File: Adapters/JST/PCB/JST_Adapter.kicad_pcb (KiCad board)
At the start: 2 copper layers, 30.8 x 38 mm, 8 parts, among them J1 S4B-PH-SM4-TB(LF)(SN), J2 S6B-PH-SM4-TB(LF)(SN), P1 CONN_02X08

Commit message: adapter finished
finished adapter
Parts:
- moved FD3 32.1 mm to (101.2, 25.2)
- moved FD2 15.5 mm to (116.8, 25.2)
- moved FD1 1.50 mm to (116.8, 60.8)
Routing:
- net GND: track 0.00 -> 137.8 mm, vias 0 -> 17
- net /SPI2_NSS: track 0.00 -> 40.5 mm
- net /SPI2_SCLK: track 0.00 -> 39.8 mm
- net /SPI2_MISO: track 0.00 -> 37.3 mm
- net /SPI2_MOSI: track 0.00 -> 35.8 mm
- net /VIN: track 0.00 -> 33.4 mm
- net /USART1_RX: track 0.00 -> 20.6 mm
- net /USART1_TX: track 0.00 -> 16.0 mm
- added copper zone on B.Cu, net GND
- added copper zone on F.Cu, net GND
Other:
- net class Default: clearance 0.2 -> 0.1524; trace_width 0.25 -> 0.1524; via_dia 0.8 -> 0.635; via_drill 0.4 -> 0.3302
- rule trace_clearance: 0.2 -> 0.1524
- rule trace_min: 0.2 -> 0.1524
- rule via_min_drill: 0.3 -> 0.3302
- rule via_min_size: 0.4 -> 0.635
- board text added: "GND"
- board text added: "S1G-RF USART/SPI Adapter CERN OSHWL v1.2 Nov 2016 Designed by adamjvr"
- board text added: "SPI_MISO"
- board text added: "SPI_MOSI"
- board text added: "SPI_NSS"
- board text added: "SPI_SCLK"
- board text added: "USART_RX"
- board text added: "USART_TX"
- board text added: "VIN"

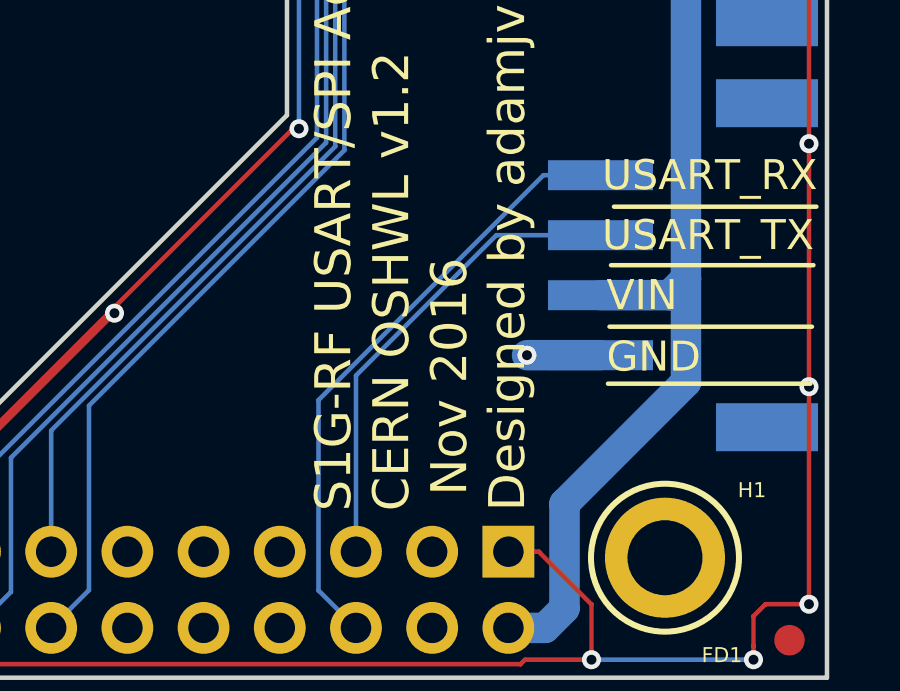
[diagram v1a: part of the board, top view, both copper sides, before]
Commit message: Via Stitching
Ground pour stiching applied to the combined PA/LNA match version of the
915MHZ radio. All ground pours and layers are now stiched together
effectively.
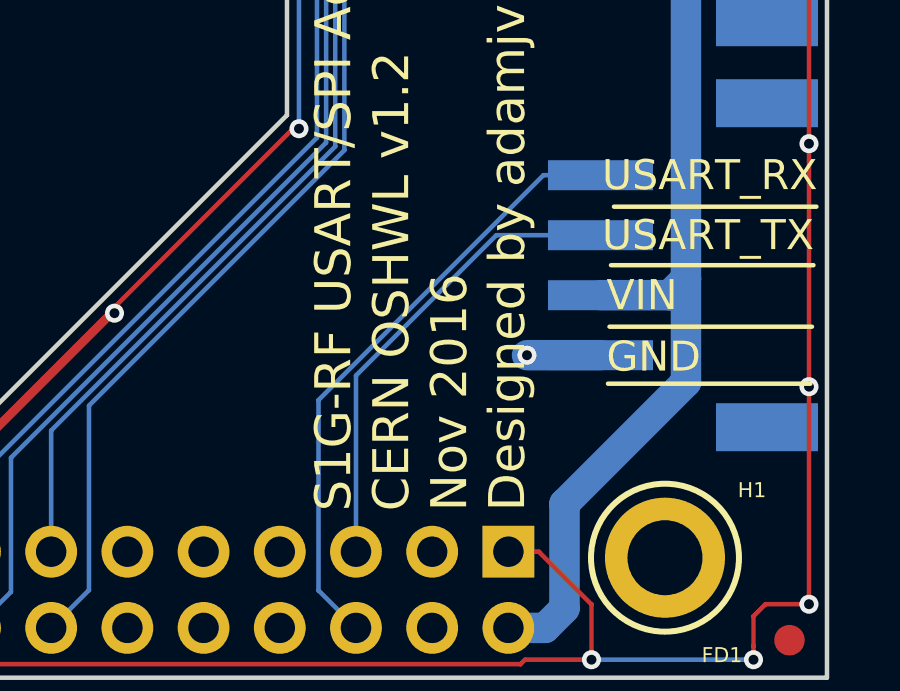
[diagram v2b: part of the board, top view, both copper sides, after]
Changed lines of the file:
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@@
   (gr_line (start 110.85 30.7) (end 117.6 30.7) (layer F.SilkS) (width 0.15))
   (gr_line (start 110.95 28.75) (end 117.7 28.75) (layer F.SilkS) (width 0.15))
-  (gr_text "S1G-RF USART/SPI Adapter\nCERN OSHWL v1.2\n Nov 2016\nDesigned by adamjvr" (at 104.45 56.45 90) (layer F.SilkS)
+  (gr_text "S1G-RF USART/SPI Adapter\nCERN OSHWL v1.2\nNov 2016\nDesigned by adamjvr" (at 104.45 56.45 90) (layer F.SilkS)
     (effects (font (size 1.2 1.2) (thickness 0.25)) (justify left))
   )

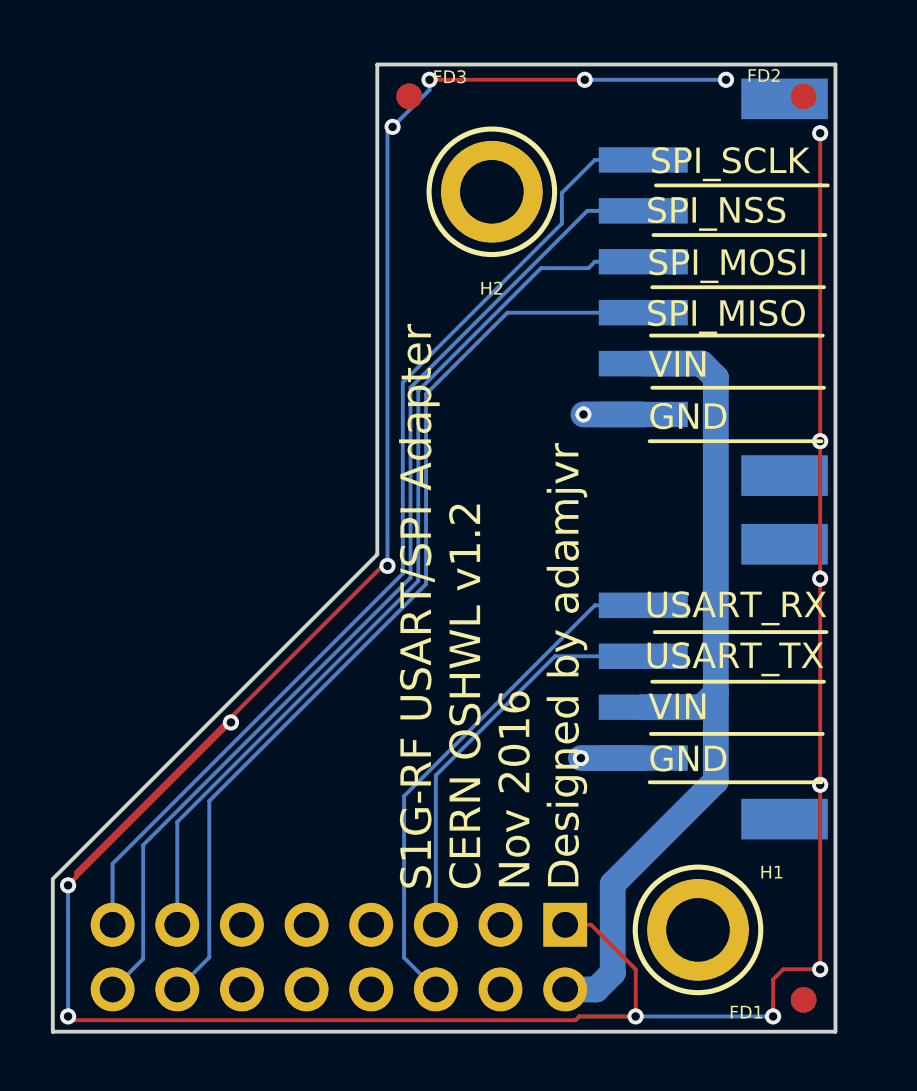
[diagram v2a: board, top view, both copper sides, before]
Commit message: Adapters
Adapter ended up being too large. So I split it into two separate
adapters one for SPI and one for USART over JST connectors. SPI board
has 100 ohm inline resistors for EMI and impedance matching in case the
driving device lacks these internally or on its board.  Additional
Fudicials added to the combined implementation.
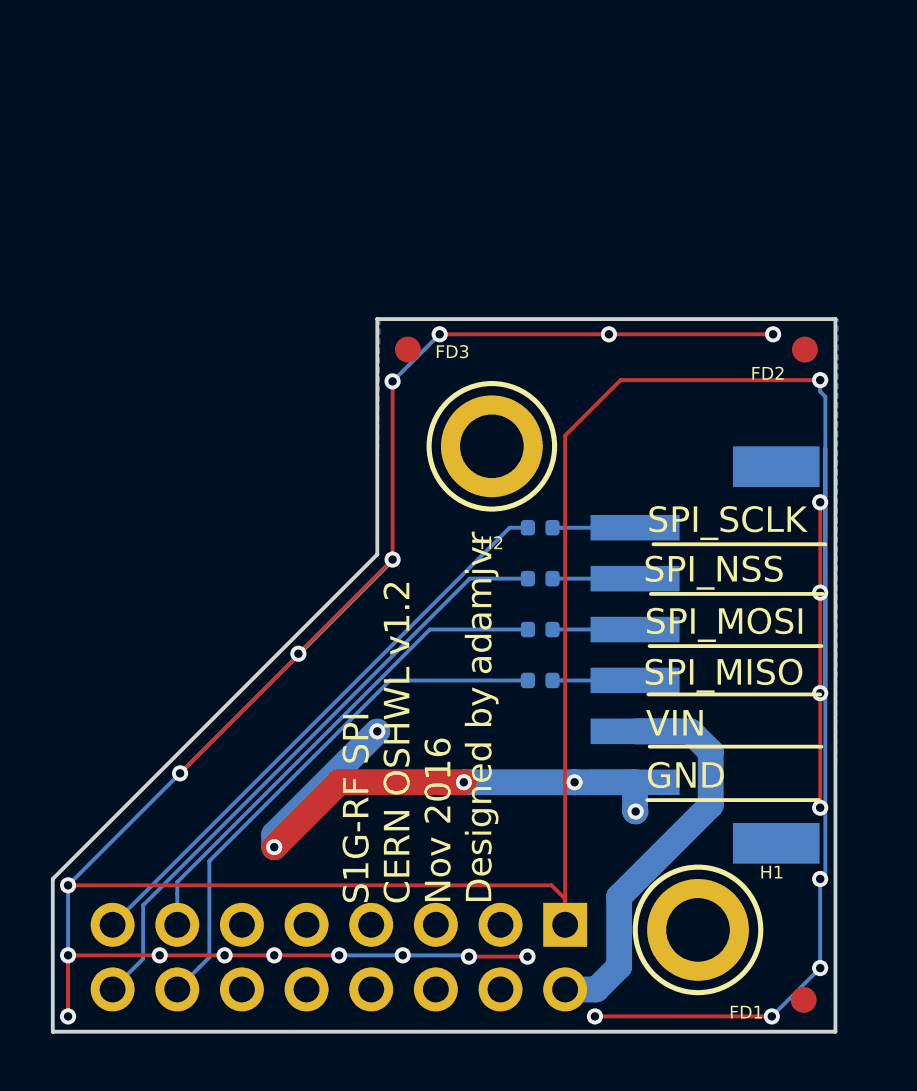
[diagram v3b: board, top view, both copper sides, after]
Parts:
- removed J2: S6B-PH-SM4-TB(LF)(SN), PCB_Footprints:S6B-PH-SM4-TB(LF)(SN)
- added R1: TNPW0402100RBEED, PCB_Footprints:R0402, B.Cu at (106.4, 42.2)
- added R2: TNPW0402100RBEED, PCB_Footprints:R0402, B.Cu at (106.4, 44.2)
- added R3: TNPW0402100RBEED, PCB_Footprints:R0402, B.Cu at (106.4, 46.2)
- added R4: TNPW0402100RBEED, PCB_Footprints:R0402, B.Cu at (106.4, 48.2)
- J1: value S4B-PH-SM4-TB(LF)(SN) -> S6B-PH-SM4-TB(LF)(SN); footprint PCB_Footprints:S4B-PH-SM4-TB(LF)(SN) -> PCB_Footprints:S6B-PH-SM4-TB(LF)(SN)
- moved H2 10.0 mm to (104.5, 39.0)
- moved FD2 9.95 mm to (116.8, 35.2)
- moved FD3 9.95 mm to (101.2, 35.2)
- moved J1 1.10 mm to (112.9, 47.2)
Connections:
- J1 pad 1: /USART1_RX -> Net-(J1-Pad1)
- J1 pad 2: /USART1_TX -> Net-(J1-Pad2)
- J1 pad 3: /VIN -> Net-(J1-Pad3)
- J1 pad 4: GND -> Net-(J1-Pad4)
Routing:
- net GND: track 137.8 -> 206.6 mm, vias 17 -> 31
- net /USART1_RX: track 20.6 -> 0.00 mm
- net /VIN: track 33.4 -> 15.7 mm, vias 0 -> 1
- net /SPI2_SCLK: track 39.8 -> 22.8 mm
- net /SPI2_NSS: track 40.5 -> 24.2 mm
- net /SPI2_MOSI: track 35.8 -> 19.6 mm
- net /SPI2_MISO: track 37.3 -> 21.0 mm
- net /USART1_TX: track 16.0 -> 0.00 mm
- net Net-(J1-Pad4): track 0.00 -> 3.24 mm
- net Net-(J1-Pad3): track 0.00 -> 3.24 mm
- net Net-(J1-Pad2): track 0.00 -> 3.24 mm
- net Net-(J1-Pad1): track 0.00 -> 3.24 mm
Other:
- board size 30.8 x 38 mm -> 30.8 x 28 mm
- board text added: "S1G-RF SPI CERN OSHWL v1.2 Nov 2016 Designed by adamjvr"
- board text removed: "S1G-RF USART/SPI Adapter CERN OSHWL v1.2 Nov 2016 Designed by adamjvr"
- board text removed: "USART_RX"
- board text removed: "USART_TX"
